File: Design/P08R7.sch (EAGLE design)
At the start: 26 parts, among them P1 PENTABIT_17.32, U1 STM32G0B1CEU6N, U2 VL53L1CXV0FY_1, X1 XTALL_CSTCE8M00G52

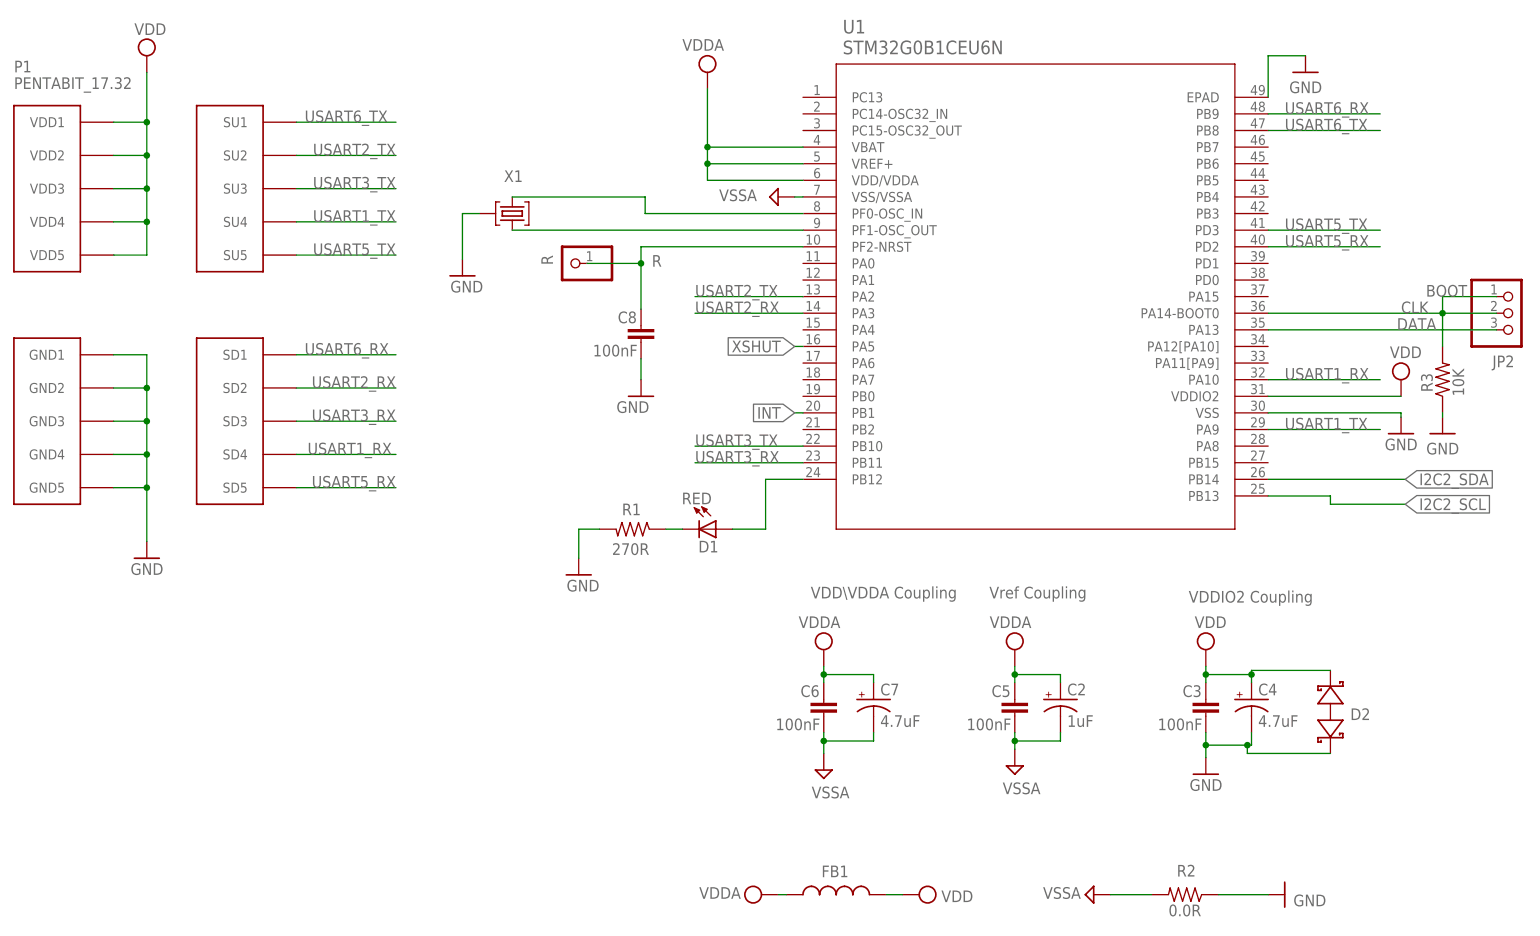
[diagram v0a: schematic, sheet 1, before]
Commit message: -Add TVS diode -Change the MCU to STM32G0B1CEU6 -Activate the thermal option for the polygon
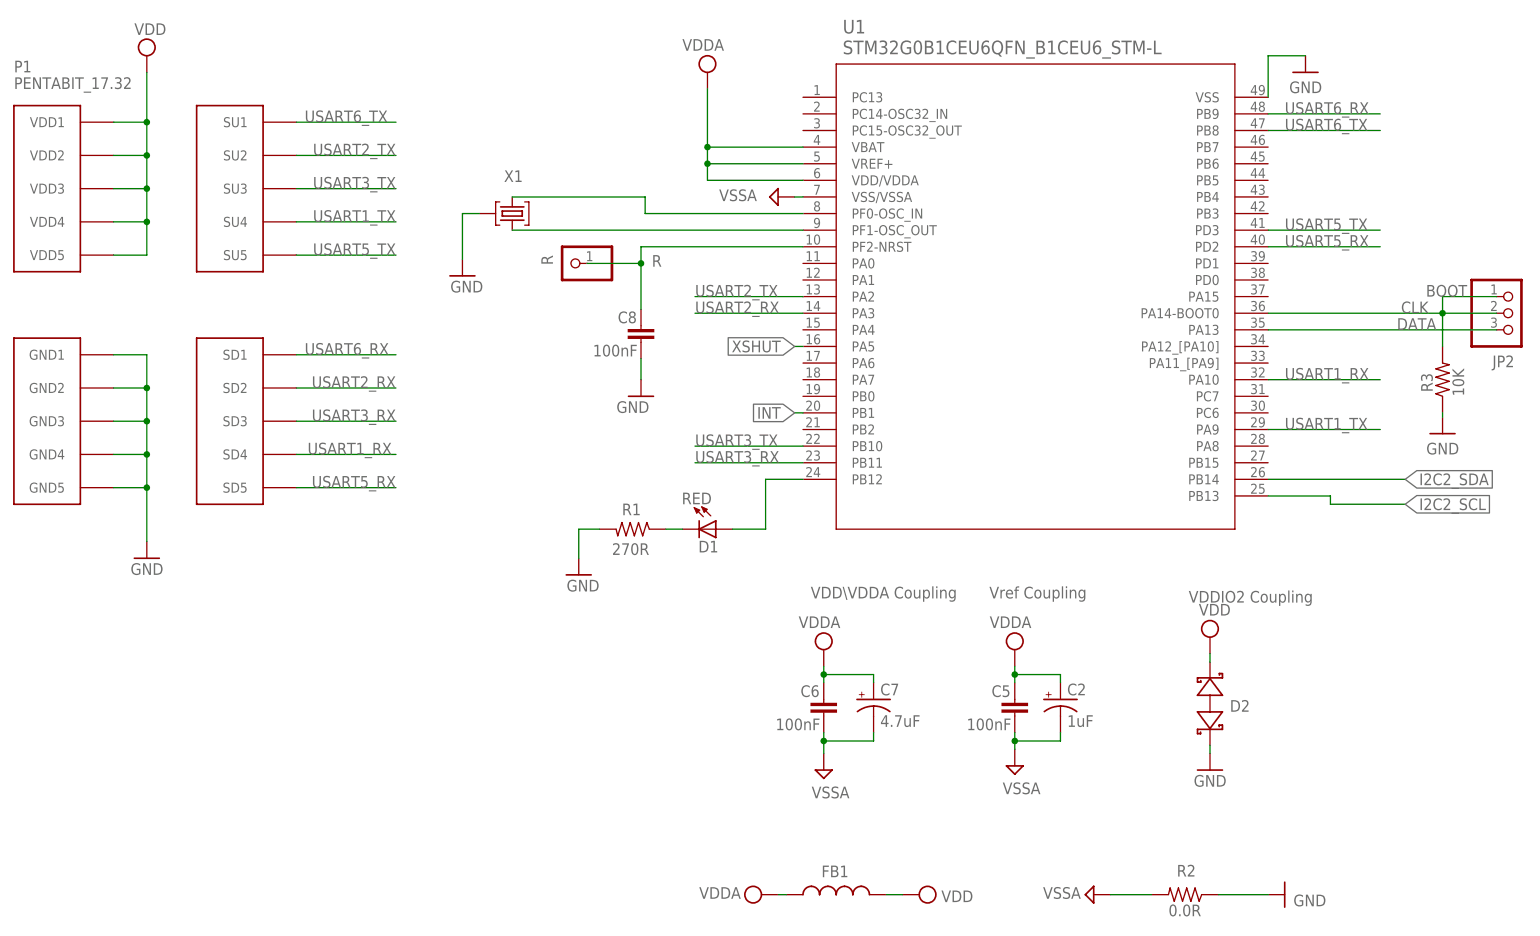
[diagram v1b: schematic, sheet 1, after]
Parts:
- removed C3: 100nF, HEXABITZ_RCLS:C-0603
- removed C4: 4.7uF, HEXABITZ_RCLS:C-0805-POL
- U1: value STM32G0B1CEU6N -> STM32G0B1CEU6QFN_B1CEU6_STM-L; device HEXABITZ_ICs:STM32G0B1CEU6N -> HEXABITZ_ICs:STM32G0B1CEU6QFN_B1CEU6_STM-L
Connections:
- net GND: no longer C3.2, C4.-, U1.EPAD
- net VDD: no longer C3.1, C4.+, U1.VDDIO2
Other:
- moved on the sheet: D2
